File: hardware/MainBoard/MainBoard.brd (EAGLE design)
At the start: 90 x 56 mm, 220 parts, among them J1 CON-71741-2184-BOT, J2 CON-71741-2184-TOP, J3 CON-FTSH-105-01-L-DV-K, J4 CON-ZX62R-B-5P, J5 CON-SMA, J6 CON-SMA, J7 CON-RJ45-J0G-0007NL, J8 SWITCH-CJS-1200-1200, M1 MOUNT-HOLE3.3, M2 MOUNT-HOLE3.3, M3 MOUNT-HOLE3.3, M4 MOUNT-HOLE3.3, M5 FIDUCIAL1X2, M6 FIDUCIAL1X2, M7 FIDUCIAL1X2, M8 FIDUCIAL1X2, Q1 MMBT3904, SW1 SWITCH-KSC-201J, SW2 SWITCH-KSC-201J, U1 A2F500M3G-FG256, U2 MAX19706-T4877-4, U3 MAX19706-T4877-4, U4 USBLC6-2SC6, U5 FT232HL, U6 DP83848C-VBH48A, U7 93LC56BT-OT, U8 DS1818-10-SOT-23, U9 LMV112, X1 FOX924B, X2 ECX-31B, X3 ASEM1-C, X5 ECX-42-120

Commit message: Removed everything from GND and SUP layers.
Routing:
- net VJTAG: vias 3 -> 4
- net TRST: vias 3 -> 2

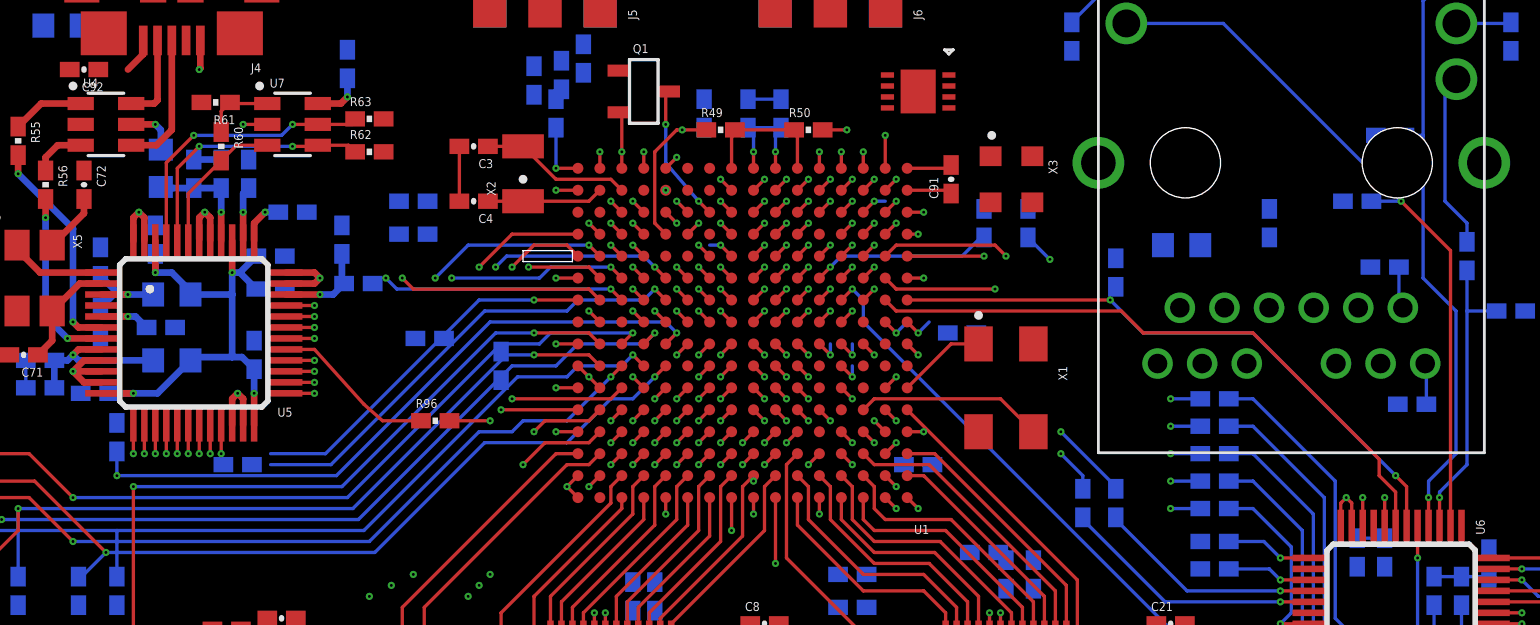
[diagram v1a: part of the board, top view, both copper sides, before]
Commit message: Routed the SF AFE signals around the BGA grid.
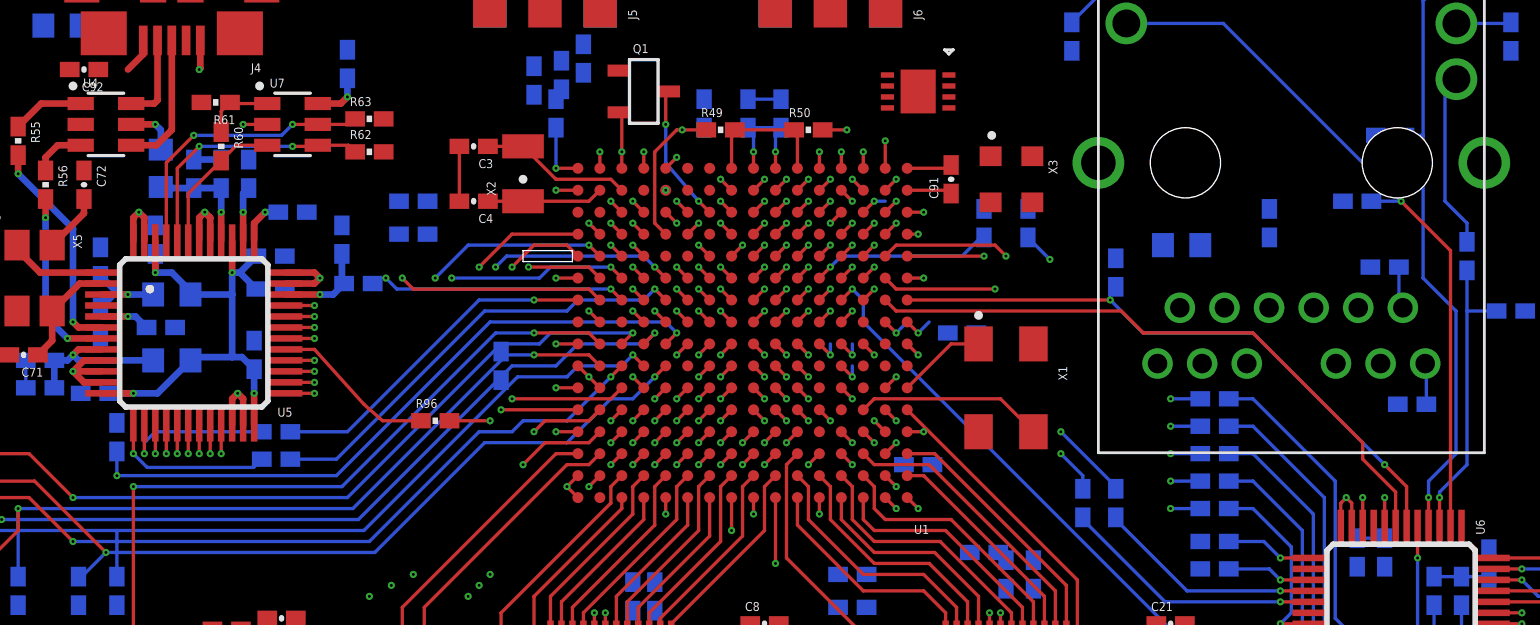
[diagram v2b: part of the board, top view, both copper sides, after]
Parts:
- moved R3 8.19 mm to (23.8, 33.5)
- moved R4 1.77 mm to (23.8, 32.2)
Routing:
- net USB_DB1: track 34.8 -> 40.9 mm
- net USB_DB0: track 35.6 -> 41.5 mm
- net SF_ABPS0: track 51.9 -> 56.0 mm
- net SF_ADC0: track 47.2 -> 49.0 mm
- net UART0_TXD: track 16.9 -> 15.6 mm
- net SF_ADC1: track 43.2 -> 44.2 mm
- net UART0_RXD: track 21.5 -> 20.5 mm
- net SF_ADC4: track 42.4 -> 41.5 mm, vias 3 -> 2
- net SF_ADC2: track 42.1 -> 42.8 mm

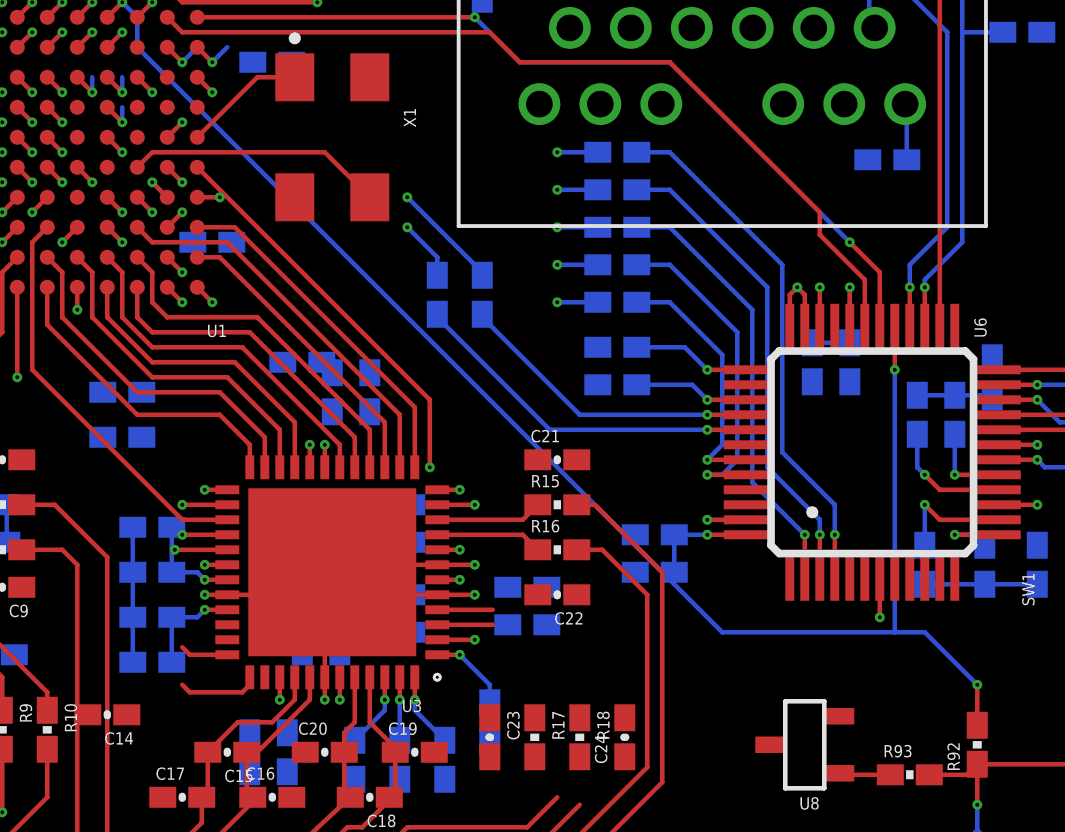
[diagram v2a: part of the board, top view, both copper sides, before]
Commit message: Minor updates on the connector on the schematic.
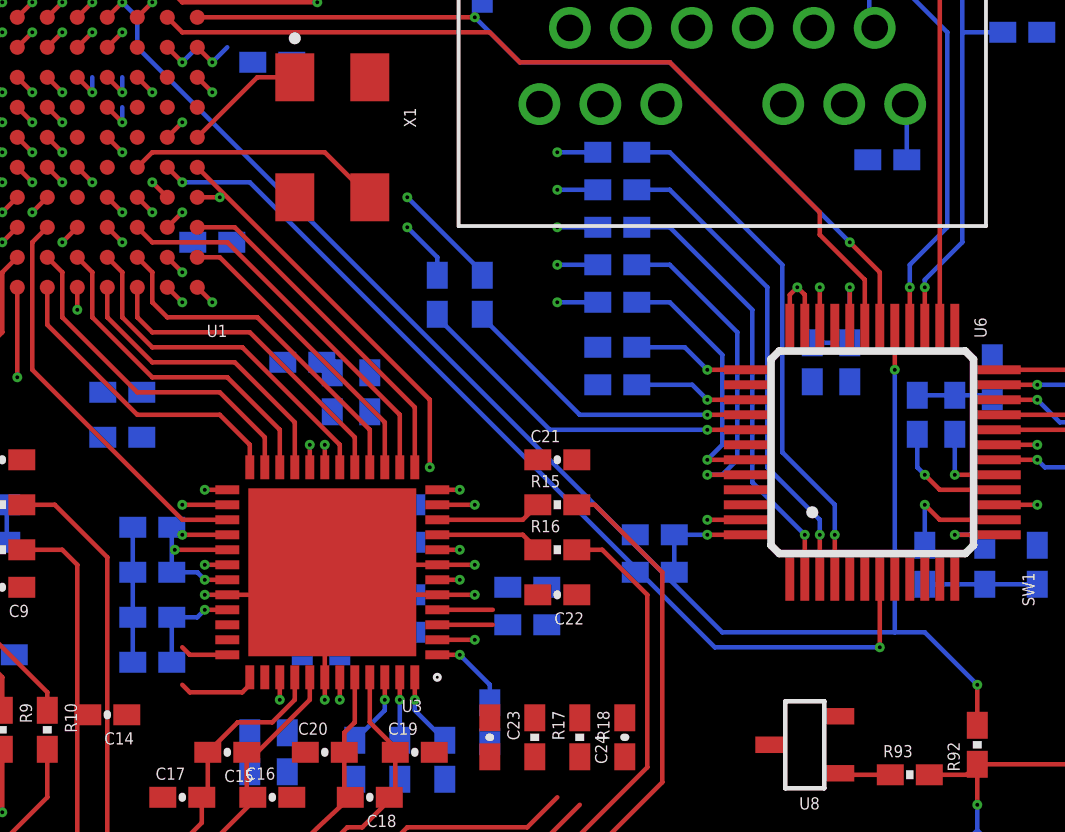
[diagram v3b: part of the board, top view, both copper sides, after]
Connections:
- net N$10 renamed NGPIO4
- net N$2 renamed NGPIO3
- net N$3 renamed NGPIO0
- net N$5 renamed NGPIO1
- net N$7 renamed NGPIO2
- removed net N$1: J2.15
- new net SGPIO0: J1.23
- new net SGPIO1: J1.21
- new net SGPIO2: J1.19
- new net SGPIO3: J1.17
- net DGND: now also J1.15, J1.16, J2.15
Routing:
- net !MAC_PWDN: track 31.3 -> 32.7 mm
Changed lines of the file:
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@@
 <layers>
 <layer number="1" name="Top" color="4" fill="1" visible="yes" active="yes"/>
-<layer number="2" name="GND" color="1" fill="3" visible="no" active="yes"/>
+<layer number="2" name="GND" color="1" fill="3" visible="yes" active="yes"/>
 <layer number="3" name="Inner1" color="13" fill="3" visible="yes" active="yes"/>
 <layer number="14" name="Inner2" color="10" fill="6" visible="yes" active="yes"/>
-<layer number="15" name="SUP" color="4" fill="6" visible="no" active="yes"/>
+<layer number="15" name="SUP" color="4" fill="6" visible="yes" active="yes"/>
 <layer number="16" name="Bottom" color="1" fill="1" visible="yes" active="yes"/>
-<layer number="17" name="Pads" color="2" fill="1" visible="no" active="yes"/>
+<layer number="17" name="Pads" color="2" fill="1" visible="yes" active="yes"/>
 <layer number="18" name="Vias" color="2" fill="1" visible="yes" active="yes"/>
-<layer number="19" name="Unrouted" color="6" fill="1" visible="no" active="yes"/>
+<layer number="19" name="Unrouted" color="6" fill="1" visible="yes" active="yes"/>
 <layer number="20" name="Dimension" color="15" fill="1" visible="yes" active="yes"/>
-<layer number="21" name="tPlace" color="7" fill="1" visible="no" active="yes"/>
+<layer number="21" name="tPlace" color="7" fill="1" visible="yes" active="yes"/>
 <layer number="22" name="bPlace" color="7" fill="1" visible="no" active="yes"/>
-<layer number="23" name="tOrigins" color="15" fill="1" visible="no" active="yes"/>
-<layer number="24" name="bOrigins" color="15" fill="1" visible="yes" active="yes"/>
-<layer number="25" name="tNames" color="7" fill="1" visible="no" active="yes"/>
+<layer number="23" name="tOrigins" color="15" fill="1" visible="yes" active="yes"/>
+<layer number="24" name="bOrigins" color="15" fill="1" visible="no" active="yes"/>
+<layer number="25" name="tNames" color="7" fill="1" visible="yes" active="yes"/>
 <layer number="26" name="bNames" color="7" fill="1" visible="no" active="yes"/>
-<layer number="27" name="tValues" color="7" fill="1" visible="no" active="yes"/>
+<layer number="27" name="tValues" color="7" fill="1" visible="yes" active="yes"/>
 <layer number="28" name="bValues" color="7" fill="1" visible="no" active="yes"/>
 <layer number="29" name="tStop" color="7" fill="3" visible="no" active="yes"/>
@@
 <layer number="49" name="Reference" color="7" fill="1" visible="no" active="yes"/>
 <layer number="50" name="dxf" color="7" fill="1" visible="no" active="yes"/>
-<layer number="51" name="tDocu" color="14" fill="1" visible="no" active="yes"/>
+<layer number="51" name="tDocu" color="14" fill="1" visible="yes" active="yes"/>
 <layer number="52" name="bDocu" color="11" fill="1" visible="no" active="yes"/>
 <layer number="53" name="tGND_GNDA" color="7" fill="9" visible="no" active="no"/>
@@
 <wire x1="79.2" y1="25.25" x2="80.5" y2="25.25" width="0.1524" layer="1"/>
 <via x="80.5" y="25.25" extent="1-16" drill="0.13"/>
+<contactref element="J2" pad="15"/>
+<contactref element="J1" pad="15"/>
+<contactref element="J1" pad="16"/>
 <wire x1="69" y1="42.35" x2="73.6" y2="41" width="0" layer="19" extent="16-16"/>
 <wire x1="74.85" y1="34.75" x2="73.6" y2="41" width="0" layer="19" extent="16-16"/>
@@
 <wire x1="24.5" y1="10.5" x2="11" y2="18.1" width="0" layer="19" extent="1-1"/>
 <wire x1="31.5" y1="10.5" x2="28.5" y2="10.5" width="0" layer="19" extent="16-16"/>
+<wire x1="31.5" y1="8.85" x2="31.5" y2="8.85" width="0" layer="19" extent="1-16"/>
+<wire x1="31.5" y1="5.15" x2="28.5" y2="5.15" width="0" layer="19" extent="1-1"/>
+<wire x1="31.5" y1="5.15" x2="31.5" y2="5.15" width="0" layer="19" extent="1-16"/>
 </signal>
 <signal name="D1V5">
@@
 <via x="51" y="34" extent="1-16" drill="0.13"/>
 <wire x1="39.5" y1="47.9" x2="39.35" y2="48.05" width="0.1524" layer="1"/>
-<wire x1="49" y1="43" x2="52.5" y2="43.5" width="0" layer="19" extent="1-1"/>
-<wire x1="49" y1="44" x2="49.5" y2="43.5" width="0" layer="19" extent="1-1"/>
-<wire x1="49.5" y1="45.5" x2="49" y2="43" width="0" layer="19" extent="1-1"/>
-<wire x1="48" y1="42" x2="48.5" y2="43.5" width="0" layer="19" extent="1-1"/>
+<wire x1="49.5" y1="43.5" x2="52.5" y2="43.5" width="0" layer="19" extent="1-1"/>
+<wire x1="48.5" y1="43.5" x2="49" y2="43" width="0" layer="19" extent="1-1"/>
+<wire x1="48" y1="42" x2="49" y2="43" width="0" layer="19" extent="1-1"/>
 <wire x1="47" y1="42" x2="47.5" y2="41.5" width="0" layer="19" extent="1-1"/>
 <wire x1="46.5" y1="42.5" x2="47" y2="42" width="0" layer="19" extent="1-1"/>
 <wire x1="46" y1="42" x2="46.5" y2="41.5" width="0" layer="19" extent="1-1"/>
+<wire x1="49.5" y1="45.5" x2="49" y2="44" width="0" layer="19" extent="1-1"/>
 <wire x1="43.5" y1="41.5" x2="45.5" y2="41.5" width="0" layer="19" extent="1-1"/>
 <wire x1="42.5" y1="42.5" x2="43" y2="42" width="0" layer="19" extent="1-1"/>
@@
 <wire x1="51.5" y1="3.5" x2="51.5" y2="11" width="0.1524" layer="14"/>
 <wire x1="51.5" y1="11" x2="51.5" y2="12.5" width="0" layer="19" extent="14-14"/>
-<wire x1="24.65" y1="19" x2="51.5" y2="12.5" width="0" layer="19" extent="1-14"/>
+<wire x1="24.65" y1="19" x2="48.5" y2="31" width="0" layer="19" extent="1-14"/>
 <wire x1="20.35" y1="19" x2="24.65" y2="19" width="0" layer="19" extent="1-1"/>
 </signal>
@@
 <wire x1="48.5" y1="3.5" x2="48.5" y2="11" width="0.1524" layer="14"/>
 <wire x1="48.5" y1="11" x2="48.5" y2="12.5" width="0" layer="19" extent="14-14"/>
-<wire x1="24.65" y1="21" x2="48.5" y2="12.5" width="0" layer="19" extent="1-14"/>
+<wire x1="24.65" y1="21" x2="48.5" y2="14.5" width="0" layer="19" extent="1-14"/>
 <wire x1="20.35" y1="21" x2="24.65" y2="21" width="0" layer="19" extent="1-1"/>
 </signal>
@@
 <wire x1="44.5" y1="41.5" x2="45" y2="42" width="0.1524" layer="1"/>
 <via x="45" y="42" extent="1-16" drill="0.13"/>
-<wire x1="45" y1="42" x2="43.5" y2="42" width="0" layer="19" extent="1-16"/>
 <wire x1="45" y1="42" x2="45" y2="38" width="0.1524" layer="14"/>
 <wire x1="45" y1="38" x2="45.5" y2="37.5" width="0.1524" layer="14"/>
@@
 <wire x1="46.5" y1="5.15" x2="46.5" y2="3.5" width="0.1524" layer="1"/>
 <via x="46.5" y="3.5" extent="1-16" drill="0.13"/>
-<wire x1="46.5" y1="30.25" x2="46" y2="30.75" width="0" layer="19" extent="3-14"/>
 </signal>
 <signal name="SF_ADC5">
@@
 <wire x1="44" y1="43" x2="44" y2="42" width="0.1524" layer="14"/>
 <wire x1="44" y1="42" x2="44.5" y2="41.5" width="0.1524" layer="14"/>
-<wire x1="44.5" y1="41.5" x2="44.5" y2="33.5" width="0" layer="19" extent="1-16"/>
 <wire x1="44.5" y1="41.5" x2="44.5" y2="12" width="0.1524" layer="14"/>
 <wire x1="44.5" y1="12" x2="45.5" y2="11" width="0.1524" layer="14"/>
@@
 <via x="45.5" y="3.5" extent="1-16" drill="0.13"/>
 <wire x1="20.35" y1="23" x2="24.65" y2="23" width="0" layer="19" extent="1-1"/>
-<wire x1="44.5" y1="33.5" x2="24.65" y2="23" width="0" layer="19" extent="1-14"/>
+<wire x1="44.5" y1="12" x2="24.65" y2="23" width="0" layer="19" extent="1-14"/>
 </signal>
 <signal name="SF_ADC6">
@@
 <wire x1="45.5" y1="28.5" x2="38.25" y2="21.25" width="0.1524" layer="3"/>
 <wire x1="38.25" y1="21.25" x2="34.75" y2="21.25" width="0.1524" layer="3"/>
-<wire x1="38.25" y1="21.25" x2="36.85" y2="23" width="0" layer="19" extent="14-16"/>
+<wire x1="35.5" y1="21.25" x2="36.85" y2="23" width="0" layer="19" extent="1-16"/>
 </signal>
 <signal name="!SPI1_SS_AFE2">
@@
 <wire x1="51.5" y1="34.5" x2="52" y2="34" width="0.1524" layer="1"/>
 <via x="52" y="34" extent="1-16" drill="0.13"/>
-<wire x1="52" y1="34" x2="55.25" y2="34" width="0.1524" layer="3"/>
+<wire x1="52" y1="34" x2="54.25" y2="34" width="0.1524" layer="16"/>
 <contactref element="X3" pad="1"/>
-<wire x1="75.25" y1="20.8" x2="75.25" y2="19.5" width="0.1524" layer="1"/>
-<via x="75.25" y="19.5" extent="1-16" drill="0.13"/>
-<wire x1="75.25" y1="19.5" x2="69.75" y2="19.5" width="0.1524" layer="3"/>
-<wire x1="69.75" y1="19.5" x2="55.25" y2="34" width="0.1524" layer="3"/>
-<wire x1="55.25" y1="34" x2="56.3" y2="46.05" width="0" layer="19" extent="1-3"/>
+<wire x1="75.25" y1="20.8" x2="75.25" y2="18.5" width="0.1524" layer="1"/>
+<via x="75.25" y="18.5" extent="1-16" drill="0.13"/>
+<wire x1="75.25" y1="18.5" x2="69.75" y2="18.5" width="0.1524" layer="16"/>
+<wire x1="69.75" y1="18.5" x2="54.25" y2="34" width="0.1524" layer="16"/>
+<wire x1="54.25" y1="34" x2="56.3" y2="46.05" width="0" layer="19" extent="1-3"/>
 </signal>
 <signal name="N$63">
@@
 <wire x1="30.5" y1="25.5" x2="30.5" y2="8.85" width="0.1524" layer="1"/>
 </signal>
-<signal name="N$3">
+<signal name="NGPIO0">
 <contactref element="J2" pad="21"/>
 </signal>
-<signal name="N$5">
+<signal name="NGPIO1">
 <contactref element="J2" pad="19"/>
 </signal>
-<signal name="N$7">
+<signal name="NGPIO2">
 <contactref element="J2" pad="17"/>
 </signal>
@@
 <wire x1="29.5" y1="40.5" x2="26.5" y2="37.5" width="0.1524" layer="14"/>
 </signal>
-<signal name="N$1">
-<contactref element="J2" pad="15"/>
-</signal>
-<signal name="N$2">
+<signal name="NGPIO3">
 <contactref element="J2" pad="13"/>
 </signal>
-<signal name="N$10">
+<signal name="NGPIO4">
 <contactref element="J2" pad="11"/>
 </signal>
@@
 <wire x1="65.25" y1="26.25" x2="69.5" y2="26.25" width="0.1524" layer="16"/>
 </signal>
+<signal name="SGPIO0">
+<contactref element="J1" pad="23"/>
+</signal>
+<signal name="SGPIO1">
+<contactref element="J1" pad="21"/>
+</signal>
+<signal name="SGPIO2">
+<contactref element="J1" pad="19"/>
+</signal>
+<signal name="SGPIO3">
+<contactref element="J1" pad="17"/>
+</signal>
 </signals>
